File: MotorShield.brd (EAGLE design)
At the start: 85 x 56 mm, 87 parts, among them IC1 OPA4340E, IC2 OPA4340E, IC3 74HCT125D, X1 MSTBV2, X2 MSTBV8, X3 MSTBV8, X4 INPUTS, X5 BUTTON_LED, X6 DOTSTARS

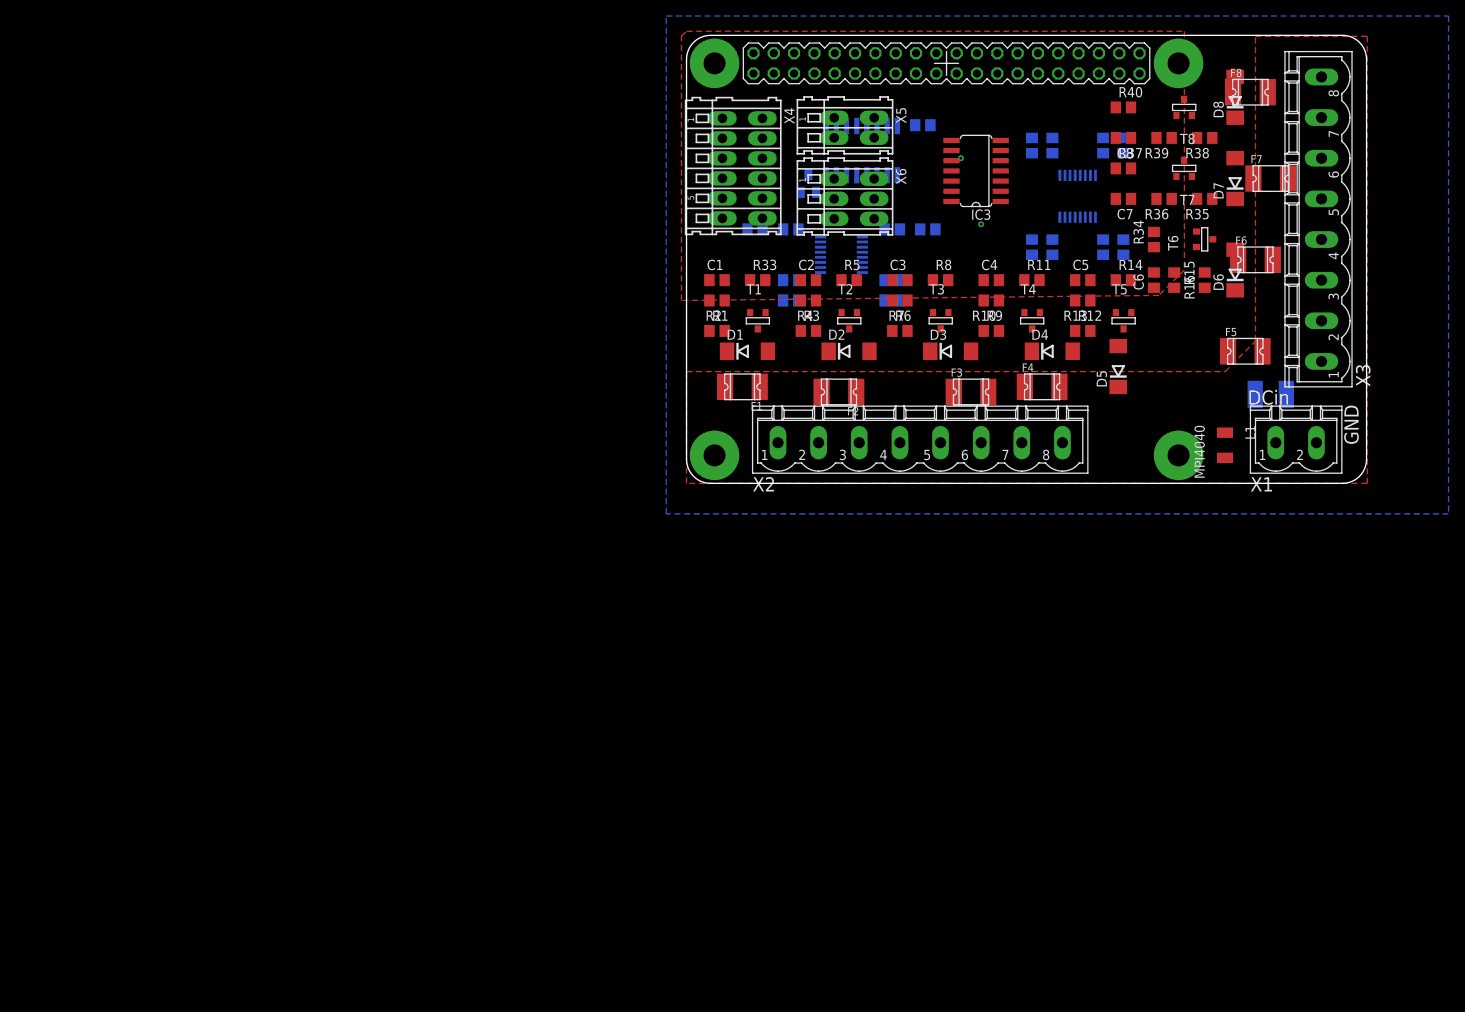
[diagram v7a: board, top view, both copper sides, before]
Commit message: added LEDs to indicate powered outputs and tripped fuses fixes #4, fixes #6
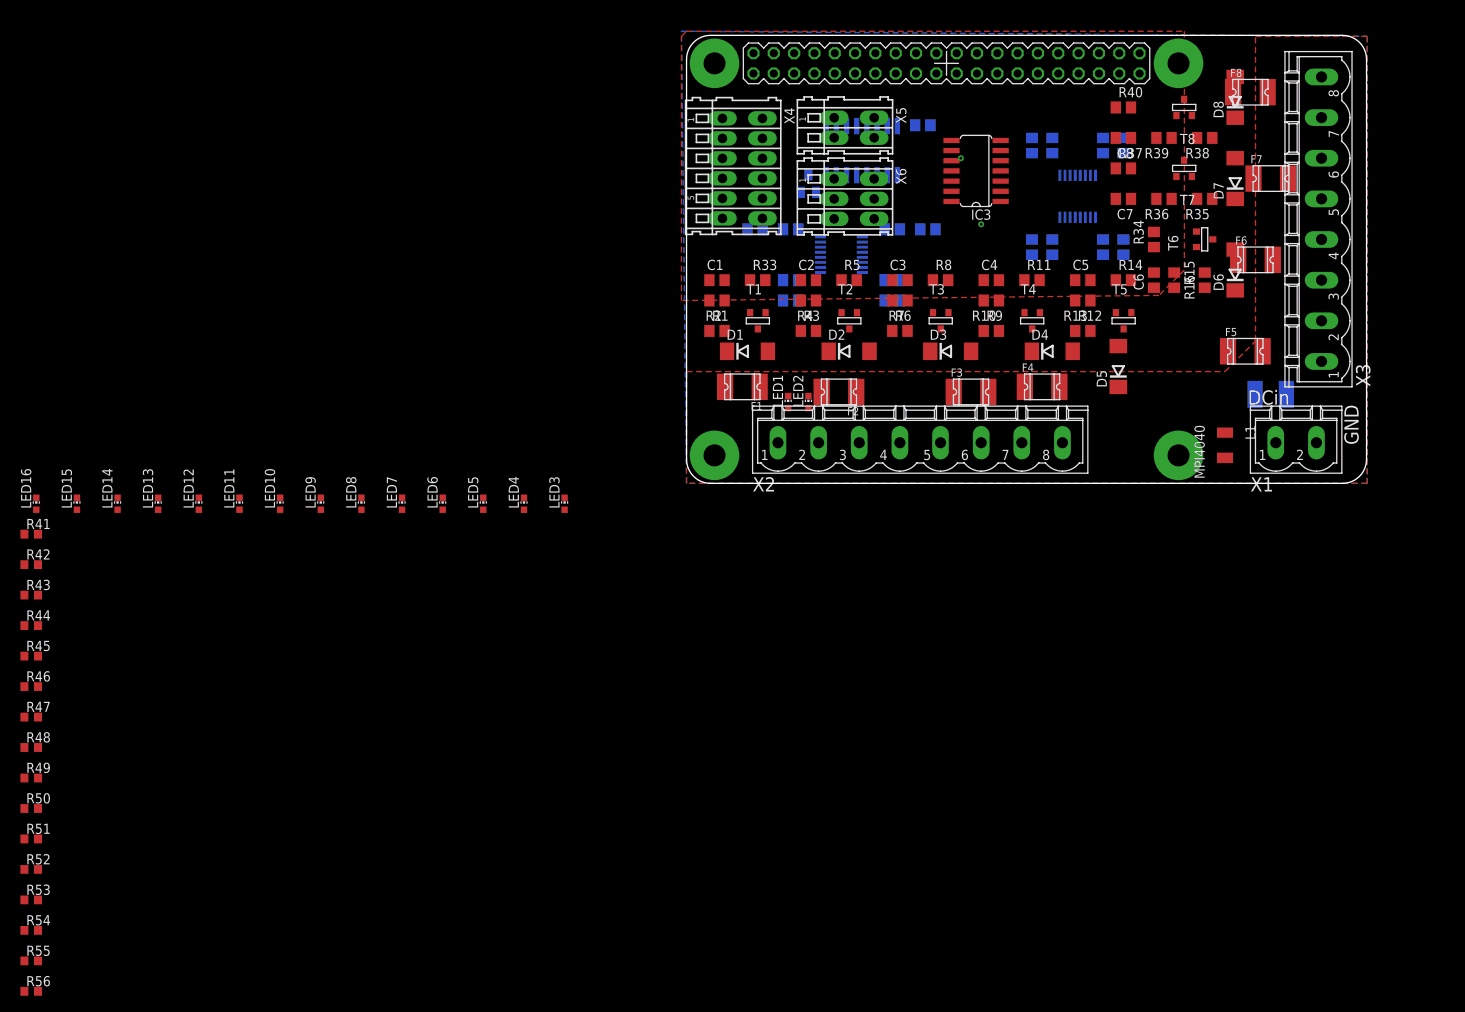
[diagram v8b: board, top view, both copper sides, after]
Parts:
- added LED1, LED11, LED13, LED15, LED3, LED5, LED7, LED9: red, led:CHIP-LED0603
- added LED10, LED12, LED14, LED16, LED2, LED4, LED6, LED8: yellow, led:CHIP-LED0603
- added R41, R42, R43, R44, R45, R46, R47, R48, R49, R50, R51, R52, R53, R54, R55, R56: (no value), rcl:R0603
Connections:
- new net N$24: LED15.A, R55.1
- new net N$25: LED16.A, R56.1
- new net N$28: LED1.A, R41.1
- new net N$30: LED2.A, R42.1
- new net N$35: LED3.A, R43.1
- new net N$36: LED4.A, R44.1
- new net N$41: LED6.A, R46.1
- new net N$42: LED5.A, R45.1
- new net N$43: LED7.A, R47.1
- new net N$44: LED8.A, R48.1
- new net N$47: LED9.A, R49.1
- new net N$48: LED10.A, R50.1
- new net N$49: LED11.A, R51.1
- new net N$50: LED12.A, R52.1
- new net N$53: LED13.A, R53.1
- new net N$54: LED14.A, R54.1
- net +24V: now also R41.2, R42.2, R43.2, R44.2, R45.2, R46.2, R47.2, R48.2, R49.2, R50.2, R51.2, R52.2, R53.2, R54.2, R55.2, R56.2
- net 24V/1A: now also LED1.C
- net N$10: now also LED4.C
- net N$12: now also LED5.C
- net N$13: now also LED3.C
- net N$17: now also LED6.C
- net N$2: now also LED2.C
- net N$26: now also LED8.C
- net N$38: now also LED10.C
- net N$4: now also LED15.C
- net N$45: now also LED12.C
- net N$5: now also LED13.C
- net N$51: now also LED14.C
- net N$57: now also LED16.C
- net N$7: now also LED11.C
- net N$8: now also LED9.C
- net N$9: now also LED7.C
